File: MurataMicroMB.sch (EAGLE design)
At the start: 10 parts, among them CON1 CON_MICROSD_C2395, CON3 CON_MIL_10_ARM, IC1 74LVC1G00DBV

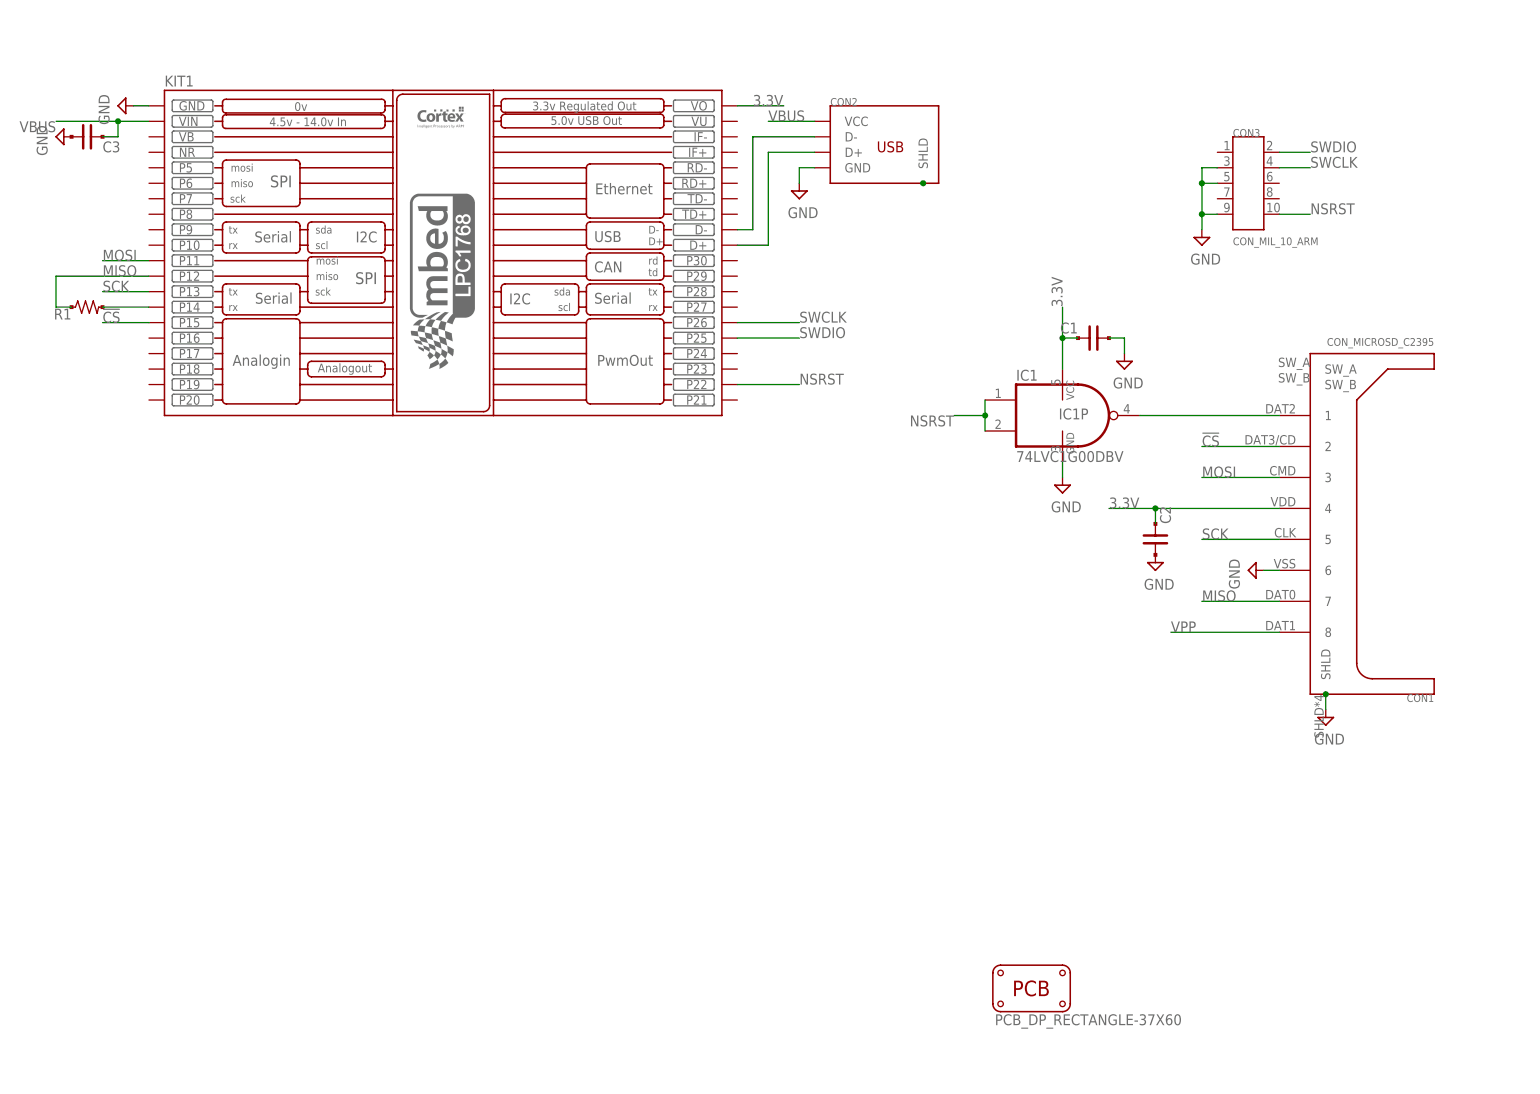
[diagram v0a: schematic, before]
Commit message: [ FIX ] add DCDC converter(for Vpp), microSD sockets, switches, USB circuit
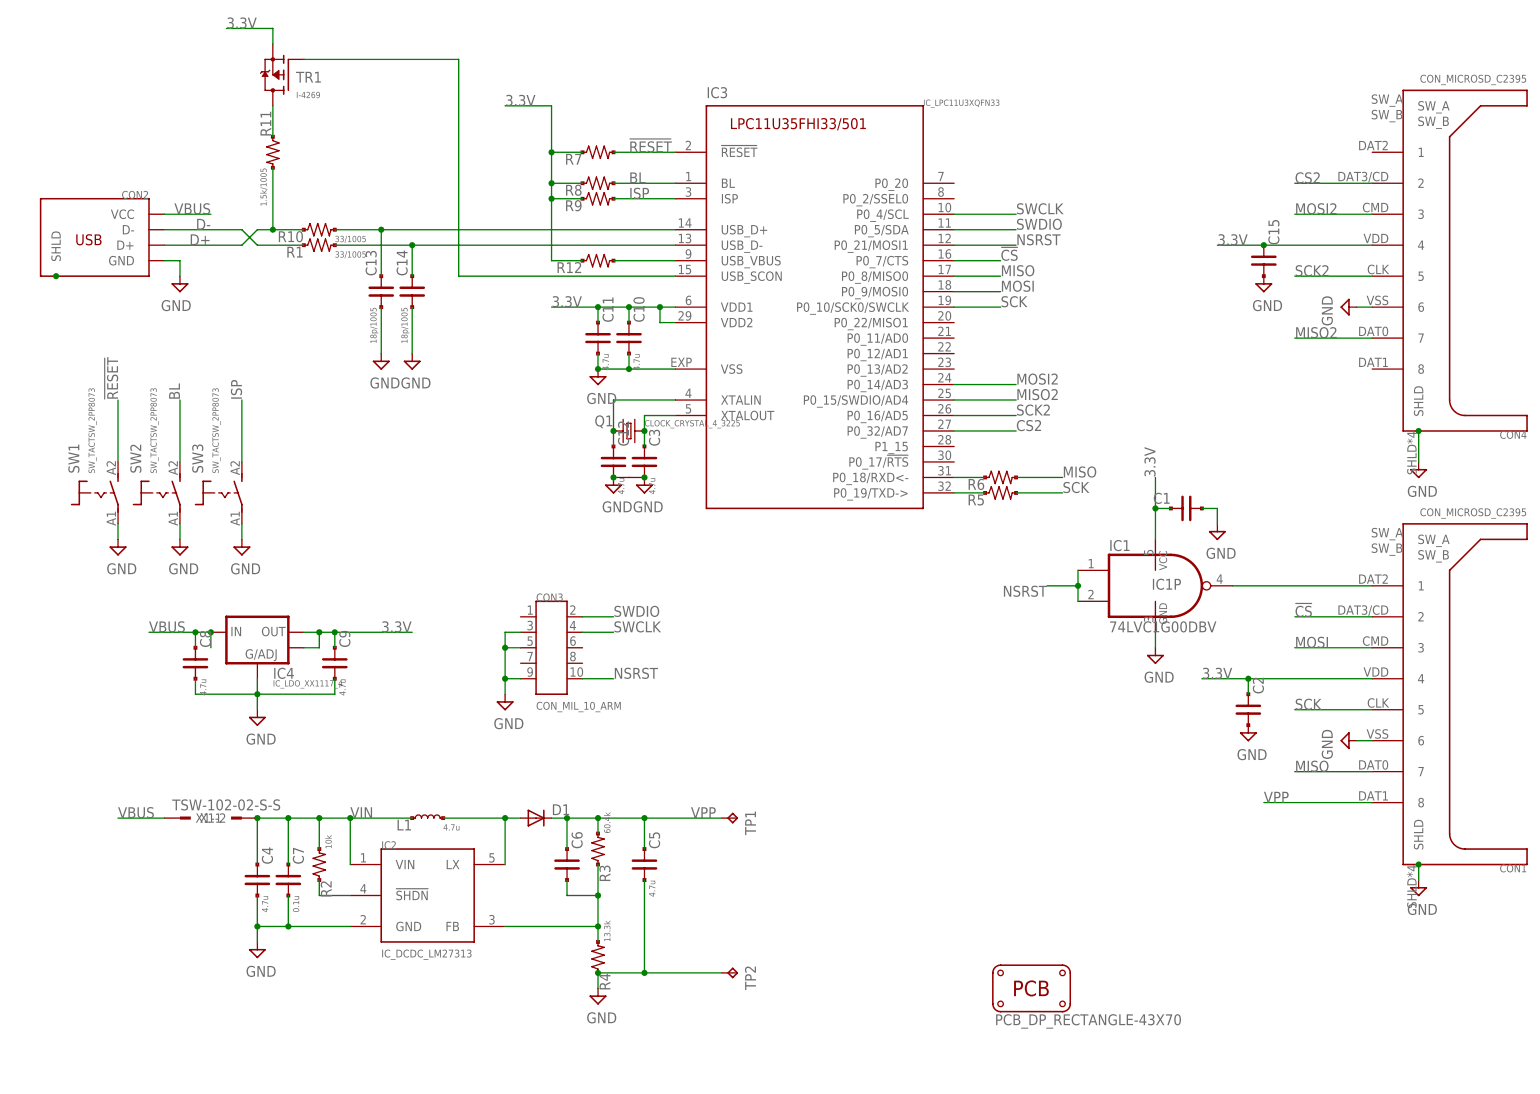
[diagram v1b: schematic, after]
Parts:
- removed KIT1: MBED_NXP_LPC1768, MBED_v2.1:MBED_NXP_LPC1768
- added C10, C11, C12: 4.7u, mylib:C_PAD_PAD_1005
- added C13, C14: 18p/1005, mylib:C_PAD_PAD_1005
- added C15, C6: (no value), mylib:C_PAD_PAD_1608
- added C4, C5, C8, C9: 4.7u, mylib:C_PAD_PAD_2125
- added C7: 0.1u, mylib:C_PAD_PAD_1608
- added CON4: CON_MICROSD_C2395, mylib:CON_MICROSD_C2395
- added D1: DIODE_SMALL, mylib:DIODE_SMALL
- added IC2: IC_DCDC_LM27313, mylib:IC_DCDC_LM27313
- added IC3: IC_LPC11U3XQFN33, mylib:IC_LPC11U3XQFN33
- added IC4: IC_LDO_XX1117_4, mylib:IC_LDO_XX1117_4
- added L1: 4.7u, mylib:INDUCTOR_2016
- added Q1: CLOCK_CRYSTAL_4_3225, mylib:CLOCK_CRYSTAL_4_3225
- added R10: 33/1005, mylib:R_US_PAD_PAD_1005
- added R11: 1.5k/1005, mylib:R_US_PAD_PAD_1005
- added R12, R5, R6, R7, R8, R9: (no value), mylib:R_US_PAD_PAD_1005
- added R2: 10k, mylib:R_US_PAD_PAD_1608
- added R3: 60.4k, mylib:R_US_PAD_PAD_1608
- added R4: 13.3k, mylib:R_US_PAD_PAD_1608
- added SW1, SW2, SW3: SW_TACTSW_2PP8073, mylib:SW_TACTSW_2PP8073
- added TP1, TP2: TPPAD1-13, testpad_local:TPPAD1-13
- added TR1: I-4269, mylib:TR_PMOS_GDS_SOT23
- added X1: TSW-102-02-S-S, con-samtec.local:TSW-102-02-S-S
- C1: device mylib:C_PAD_PAD_1608 -> mylib:C_PAD_PAD_1005
- C3: value (none) -> 4.7u; device mylib:C_PAD_PAD_1608 -> mylib:C_PAD_PAD_1005
- PCB1: value PCB_DP_RECTANGLE-37X60 -> PCB_DP_RECTANGLE-43X70; device dp_pcb:PCB_DP_RECTANGLE-37X60 -> dp_pcb:PCB_DP_RECTANGLE-43X70
- R1: value (none) -> 33/1005
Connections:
- removed net N$1: CON2.D-, KIT1.D-
- new net !RESET!: IC3.!RESET!, R7.2, SW1.S
- new net BL: IC3.BL, R8.2, SW2.S
- new net CS2: CON4.2, IC3.P0_32/AD7
- new net D+: CON2.D+, R10.1, R11.2
- new net D-: CON2.D-, R1.1
- new net ISP: IC3.ISP, R9.2, SW3.S
- new net MISO2: CON4.7, IC3.P0_15/SWDIO/AD4
- new net MOSI2: CON4.3, IC3.P0_14/AD3
- new net N$10: C6.2, IC2.FB, R3.1, R4.2
- new net N$11: C3.1, IC3.XTALOUT, Q1.2
- new net N$12: IC3.USB_SCON, TR1.G
- new net N$13: IC3.USB_VBUS, R12.2
- new net N$20: C13.1, IC3.USB_D+, R10.2
- new net N$24: C14.1, IC3.USB_D-, R1.2
- new net N$6: IC3.P0_18/RXD<-, R6.1
- new net N$7: D1.A, IC2.LX, L1.2
- new net N$8: IC2.!SHDN!, R2.1
- new net N$9: IC3.P0_19/TXD->, R5.1
- new net SCK2: CON4.5, IC3.P0_16/AD5
- new net VIN: C4.1, C7.1, IC2.VIN, L1.1, R2.2, X1-2.1
- net !CS!: now also IC3.P0_7/CTS; no longer KIT1.P15
- net 3.3V: now also C10.1, C11.1, C15.1, C9.1, CON4.4, IC3.VDD1, IC3.VDD2, IC4.OUT, IC4.OUT@1, R12.1, R7.1, R8.1, R9.1, TR1.S; no longer KIT1.VO
- net GND: now also C10.2, C11.2, C12.2, C13.2, C14.2, C15.2, C4.2, C5.2, C7.2, C8.2, C9.2, CON4.6, CON4.SHLD, IC2.GND, IC3.VSS, IC4.ADJ, Q1.P$1, Q1.P$2, R4.1, SW1.P, SW2.P, SW3.P, TP2.TP; no longer KIT1.GND
- net MISO: now also IC3.P0_8/MISO0, R6.2; no longer KIT1.P12, R1.1
- net MOSI: now also IC3.P0_9/MOSI0; no longer KIT1.P11
- net N$2: now also R11.1, TR1.D; no longer CON2.D+, KIT1.D+
- net N$5: now also C12.1, IC3.XTALIN, Q1.1; no longer KIT1.P14, R1.2
- net NSRST: now also IC3.P0_21/MOSI1; no longer KIT1.P22
- net SCK: now also IC3.P0_10/SCK0/SWCLK, R5.2; no longer KIT1.P13
- net SWCLK: now also IC3.P0_4/SCL; no longer KIT1.P26
- net SWDIO: now also IC3.P0_5/SDA; no longer KIT1.P25
- net VBUS: now also C8.1, IC4.IN, X1-1.1; no longer C3.1, KIT1.VIN
- net VPP: now also C5.1, C6.1, D1.C, R3.2, TP1.TP
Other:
- moved on the sheet: C1, C2, C3, CON1, CON2, CON3, IC1, IC1P, R1

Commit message: [ MB ][ SCH ] R/C/L values
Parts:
- C1, C15, C2: value (none) -> 0.1u
- C10, C11: value 4.7u -> 0.1u
- C12, C3: value 4.7u -> 18p
- C6: value (none) -> NM
- CON1: value CON_MICROSD_C2395 -> C-2395.MurataMicroSD
- CON4: value CON_MICROSD_C2395 -> C-2395.microSD
- L1: value 4.7u -> 4.7uH/2016
- R12, R7, R8, R9: value (none) -> 10k
- R5, R6: value (none) -> 100
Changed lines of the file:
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@@
 <parts>
 <part name="FRAME1" library="frames" deviceset="A4L-LOC" device=""/>
-<part name="CON1" library="mylib" deviceset="CON_MICROSD" device="_C2395"/>
+<part name="CON1" library="mylib" deviceset="CON_MICROSD" device="_C2395" value="C-2395.MurataMicroSD"/>
 <part name="PCB1" library="dp_pcb" deviceset="PCB_DP_RECTANGLE" device="-43X70" value="PCB_DP_RECTANGLE-43X70"/>
 <part name="IC1" library="74xx-little-us_local" deviceset="74*1G00" device="DBV" technology="LVC"/>
@@
 <part name="SUPPLY3" library="mylib" deviceset="GND" device=""/>
 <part name="SUPPLY4" library="mylib" deviceset="GND" device=""/>
-<part name="C1" library="mylib" deviceset="C_PAD_PAD_" device="1005"/>
+<part name="C1" library="mylib" deviceset="C_PAD_PAD_" device="1005" value="0.1u"/>
 <part name="SUPPLY6" library="mylib" deviceset="GND" device=""/>
-<part name="C2" library="mylib" deviceset="C_PAD_PAD_" device="1608"/>
+<part name="C2" library="mylib" deviceset="C_PAD_PAD_" device="1608" value="0.1u"/>
 <part name="SUPPLY7" library="mylib" deviceset="GND" device=""/>
 <part name="SUPPLY8" library="mylib" deviceset="GND" device=""/>
-<part name="L1" library="mylib" deviceset="INDUCTOR" device="_2016" value="4.7u"/>
+<part name="L1" library="mylib" deviceset="INDUCTOR" device="_2016" value="4.7uH/2016"/>
 <part name="IC2" library="mylib" deviceset="IC_DCDC_LM27313" device=""/>
 <part name="D1" library="mylib" deviceset="DIODE_SMALL" device=""/>
@@
 <part name="C4" library="mylib" deviceset="C_PAD_PAD_" device="2125" value="4.7u"/>
 <part name="C5" library="mylib" deviceset="C_PAD_PAD_" device="2125" value="4.7u"/>
-<part name="C6" library="mylib" deviceset="C_PAD_PAD_" device="1608"/>
+<part name="C6" library="mylib" deviceset="C_PAD_PAD_" device="1608" value="NM"/>
 <part name="SUPPLY10" library="mylib" deviceset="GND" device=""/>
 <part name="SUPPLY11" library="mylib" deviceset="GND" device=""/>
@@
 <part name="SUPPLY12" library="mylib" deviceset="GND" device=""/>
 <part name="SUPPLY13" library="mylib" deviceset="GND" device=""/>
-<part name="C10" library="mylib" deviceset="C_PAD_PAD_" device="1005" value="4.7u"/>
-<part name="C11" library="mylib" deviceset="C_PAD_PAD_" device="1005" value="4.7u"/>
-<part name="R5" library="mylib" deviceset="R_US_PAD_PAD" device="_1005"/>
-<part name="R6" library="mylib" deviceset="R_US_PAD_PAD" device="_1005"/>
-<part name="R7" library="mylib" deviceset="R_US_PAD_PAD" device="_1005"/>
-<part name="R8" library="mylib" deviceset="R_US_PAD_PAD" device="_1005"/>
-<part name="R9" library="mylib" deviceset="R_US_PAD_PAD" device="_1005"/>
+<part name="C10" library="mylib" deviceset="C_PAD_PAD_" device="1005" value="0.1u"/>
+<part name="C11" library="mylib" deviceset="C_PAD_PAD_" device="1005" value="0.1u"/>
+<part name="R5" library="mylib" deviceset="R_US_PAD_PAD" device="_1005" value="100"/>
+<part name="R6" library="mylib" deviceset="R_US_PAD_PAD" device="_1005" value="100"/>
+<part name="R7" library="mylib" deviceset="R_US_PAD_PAD" device="_1005" value="10k"/>
+<part name="R8" library="mylib" deviceset="R_US_PAD_PAD" device="_1005" value="10k"/>
+<part name="R9" library="mylib" deviceset="R_US_PAD_PAD" device="_1005" value="10k"/>
 <part name="Q1" library="mylib" deviceset="CLOCK_CRYSTAL_4" device="_3225"/>
-<part name="C3" library="mylib" deviceset="C_PAD_PAD_" device="1005" value="4.7u"/>
-<part name="C12" library="mylib" deviceset="C_PAD_PAD_" device="1005" value="4.7u"/>
+<part name="C3" library="mylib" deviceset="C_PAD_PAD_" device="1005" value="18p"/>
+<part name="C12" library="mylib" deviceset="C_PAD_PAD_" device="1005" value="18p"/>
 <part name="SUPPLY2" library="mylib" deviceset="GND" device=""/>
 <part name="IC4" library="mylib" deviceset="IC_LDO_XX1117_4" device=""/>
@@
 <part name="SUPPLY9" library="mylib" deviceset="GND" device=""/>
 <part name="SUPPLY14" library="mylib" deviceset="GND" device=""/>
-<part name="R12" library="mylib" deviceset="R_US_PAD_PAD" device="_1005"/>
+<part name="R12" library="mylib" deviceset="R_US_PAD_PAD" device="_1005" value="10k"/>
 <part name="SUPPLY15" library="mylib" deviceset="GND" device=""/>
 <part name="SW1" library="mylib" deviceset="SW_TACTSW_2P" device="P8073"/>
@@
 <part name="SUPPLY17" library="mylib" deviceset="GND" device=""/>
 <part name="SUPPLY18" library="mylib" deviceset="GND" device=""/>
-<part name="CON4" library="mylib" deviceset="CON_MICROSD" device="_C2395"/>
+<part name="CON4" library="mylib" deviceset="CON_MICROSD" device="_C2395" value="C-2395.microSD"/>
 <part name="SUPPLY19" library="mylib" deviceset="GND" device=""/>
-<part name="C15" library="mylib" deviceset="C_PAD_PAD_" device="1608"/>
+<part name="C15" library="mylib" deviceset="C_PAD_PAD_" device="1608" value="0.1u"/>
 <part name="SUPPLY20" library="mylib" deviceset="GND" device=""/>
 <part name="SUPPLY21" library="mylib" deviceset="GND" device=""/>

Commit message: [ MB ] add OSHW icon
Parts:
- added U$1: ICON_OSHW, mylib:ICON_OSHW
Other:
- note added: "r0.1"
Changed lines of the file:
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@@
 <part name="SUPPLY20" library="mylib" deviceset="GND" device=""/>
 <part name="SUPPLY21" library="mylib" deviceset="GND" device=""/>
+<part name="U$1" library="mylib" deviceset="ICON_OSHW" device=""/>
 </parts>
 <sheets>
 <sheet>
 <plain>
+<text x="162.56" y="25.4" size="15.24" layer="94">r0.1</text>
 </plain>
 <instances>
@@
 <instance part="SUPPLY20" gate="GND" x="210.82" y="127"/>
 <instance part="SUPPLY21" gate="GND" x="236.22" y="96.52"/>
+<instance part="U$1" gate="G$1" x="205.74" y="20.32"/>
 </instances>
 <busses>
@@
 <pinref part="X1" gate="-2" pin="1"/>
 <junction x="45.72" y="40.64"/>
-<label x="60.96" y="40.64" size="1.778" layer="95"/>
+<label x="63.5" y="40.64" size="1.778" layer="95"/>
 <pinref part="C7" gate="G$1" pin="1"/>
 <wire x1="50.8" y1="33.02" x2="50.8" y2="40.64" width="0.1524" layer="91"/>
